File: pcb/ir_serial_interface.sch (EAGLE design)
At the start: 22 parts, among them IC1 PIC18F2550_28W, T1 SFH303

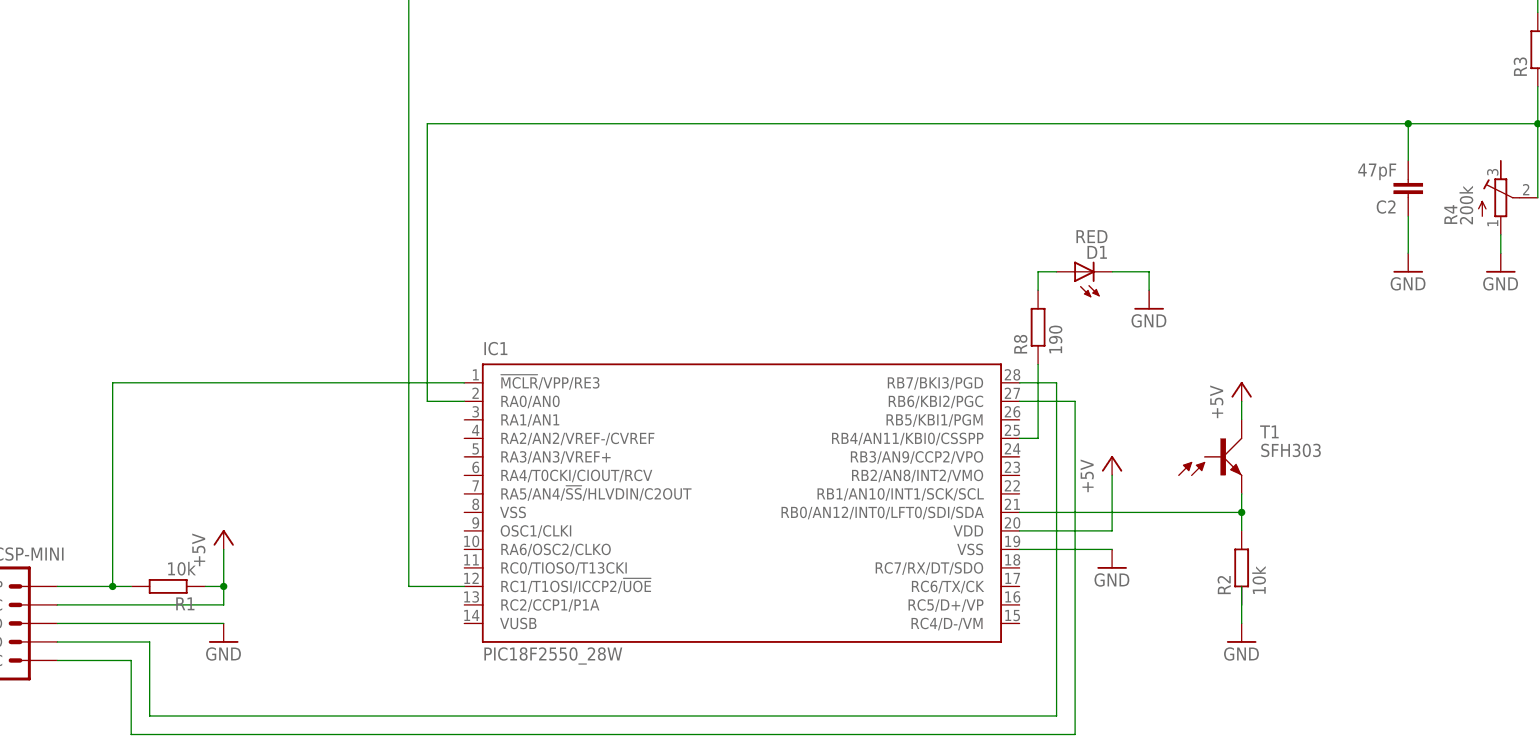
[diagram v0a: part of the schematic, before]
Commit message: RS232_TX working
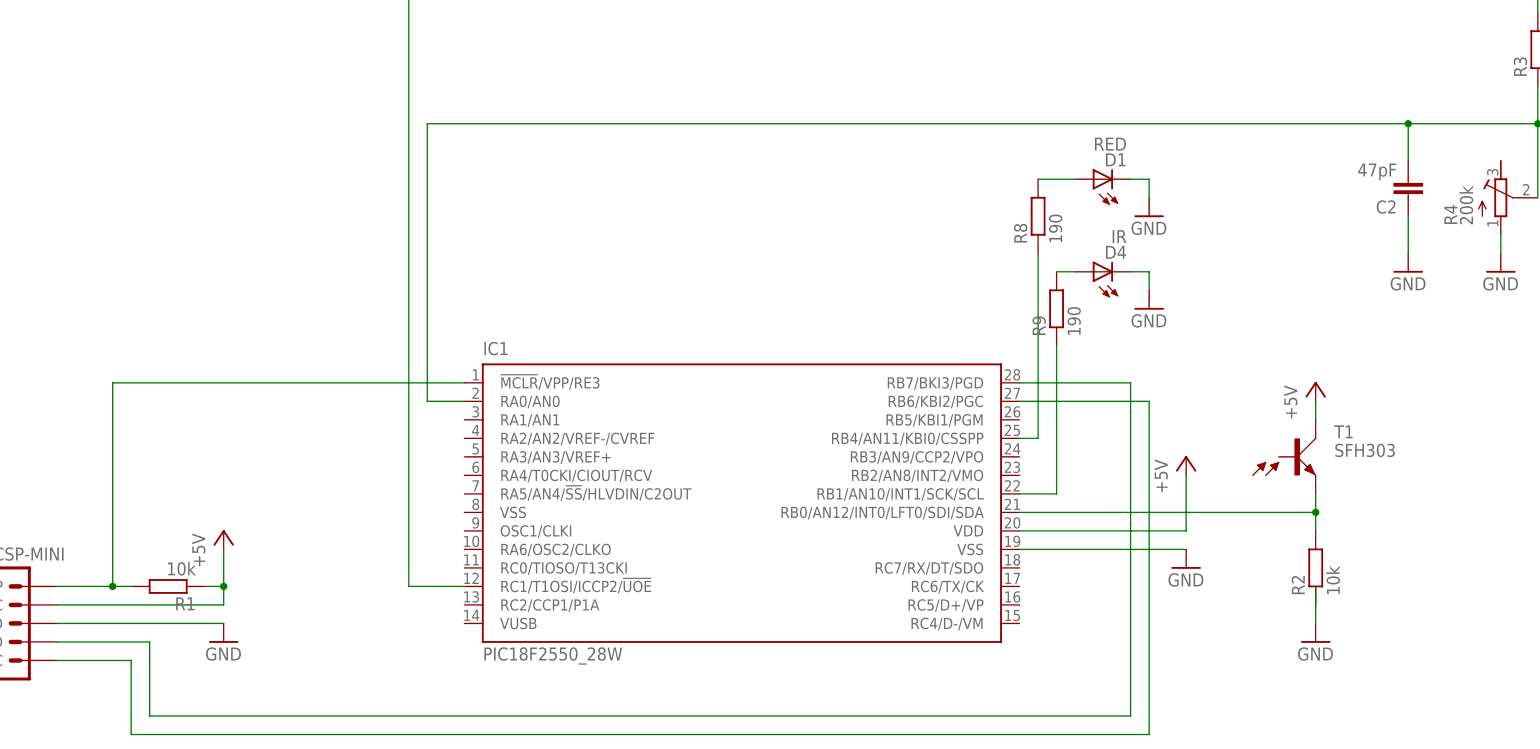
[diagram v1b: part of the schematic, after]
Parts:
- added D4: IR, led:LED3MM
- added R9: 190, resistor:R-EU_M0805
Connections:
- new net N$14: D4.A, R9.2
- new net N$15: IC1.RB1/AN10/INT1/SCK/SCL, R9.1
- net GND: now also D4.C
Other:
- moved on the sheet: D1, R2, R8, T1
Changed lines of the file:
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@@
 <?xml version="1.0" encoding="utf-8"?>
 <!DOCTYPE eagle SYSTEM "eagle.dtd">
-<eagle version="6.5.0">
+<eagle version="6.6.0">
 <drawing>
 <settings>
@@
 <part name="GND10" library="supply1" deviceset="GND" device=""/>
 <part name="R4" library="resistor" deviceset="R-TRIMM" device="3214W" value="200k"/>
+<part name="R9" library="resistor" deviceset="R-EU_" device="M0805" value="190"/>
+<part name="D4" library="led" deviceset="LED" device="3MM" value="IR"/>
+<part name="GND11" library="supply1" deviceset="GND" device=""/>
 </parts>
 <sheets>
@@
 </plain>
 <instances>
-<instance part="T1" gate="G$1" x="160.02" y="27.94"/>
-<instance part="P+1" gate="1" x="144.78" y="27.94"/>
-<instance part="GND1" gate="1" x="144.78" y="12.7"/>
-<instance part="P+2" gate="1" x="162.56" y="38.1"/>
-<instance part="GND2" gate="1" x="162.56" y="2.54"/>
-<instance part="R2" gate="G$1" x="162.56" y="12.7" rot="R90"/>
+<instance part="T1" gate="G$1" x="170.18" y="27.94"/>
+<instance part="P+1" gate="1" x="154.94" y="27.94"/>
+<instance part="GND1" gate="1" x="154.94" y="12.7"/>
+<instance part="P+2" gate="1" x="172.72" y="38.1"/>
+<instance part="GND2" gate="1" x="172.72" y="2.54"/>
+<instance part="R2" gate="G$1" x="172.72" y="12.7" rot="R90"/>
 <instance part="U$1" gate="G$1" x="-7.62" y="5.08" rot="MR0"/>
 <instance part="P+3" gate="1" x="22.86" y="17.78"/>
@@
 <instance part="GND7" gate="1" x="213.36" y="111.76"/>
 <instance part="GND8" gate="1" x="195.58" y="111.76"/>
-<instance part="D1" gate="G$1" x="139.7" y="53.34" rot="R90"/>
-<instance part="GND9" gate="1" x="149.86" y="48.26"/>
-<instance part="R8" gate="G$1" x="134.62" y="45.72" rot="R90"/>
+<instance part="D1" gate="G$1" x="142.24" y="66.04" rot="R90"/>
+<instance part="GND9" gate="1" x="149.86" y="60.96"/>
+<instance part="R8" gate="G$1" x="134.62" y="60.96" rot="R90"/>
 <instance part="BAT1" gate="G$1" x="-2.54" y="114.3"/>
 <instance part="D2" gate="G$1" x="12.7" y="114.3" rot="R180"/>
@@
 <instance part="GND10" gate="1" x="30.48" y="106.68"/>
 <instance part="R4" gate="G$1" x="198.12" y="63.5"/>
+<instance part="R9" gate="G$1" x="137.16" y="48.26" rot="R90"/>
+<instance part="D4" gate="G$1" x="142.24" y="53.34" rot="R90"/>
+<instance part="GND11" gate="1" x="149.86" y="48.26"/>
 </instances>
 <busses>
@@
 <pinref part="P+2" gate="1" pin="+5V"/>
 <pinref part="T1" gate="G$1" pin="C"/>
-<wire x1="162.56" y1="35.56" x2="162.56" y2="33.02" width="0.1524" layer="91"/>
+<wire x1="172.72" y1="35.56" x2="172.72" y2="33.02" width="0.1524" layer="91"/>
 </segment>
 <segment>
@@
 <segment>
 <pinref part="P+1" gate="1" pin="+5V"/>
-<wire x1="144.78" y1="25.4" x2="144.78" y2="17.78" width="0.1524" layer="91"/>
+<wire x1="154.94" y1="25.4" x2="154.94" y2="17.78" width="0.1524" layer="91"/>
 <pinref part="IC1" gate="G$1" pin="VDD"/>
-<wire x1="144.78" y1="17.78" x2="132.08" y2="17.78" width="0.1524" layer="91"/>
+<wire x1="154.94" y1="17.78" x2="132.08" y2="17.78" width="0.1524" layer="91"/>
 </segment>
 <segment>
@@
 <pinref part="GND2" gate="1" pin="GND"/>
 <pinref part="R2" gate="G$1" pin="1"/>
-<wire x1="162.56" y1="5.08" x2="162.56" y2="7.62" width="0.1524" layer="91"/>
-<wire x1="162.56" y1="7.62" x2="162.56" y2="10.16" width="0.1524" layer="91"/>
+<wire x1="172.72" y1="5.08" x2="172.72" y2="7.62" width="0.1524" layer="91"/>
+<wire x1="172.72" y1="7.62" x2="172.72" y2="10.16" width="0.1524" layer="91"/>
 </segment>
 <segment>
@@
 <pinref part="GND1" gate="1" pin="GND"/>
 <pinref part="IC1" gate="G$1" pin="VSS@1"/>
-<wire x1="144.78" y1="15.24" x2="132.08" y2="15.24" width="0.1524" layer="91"/>
+<wire x1="154.94" y1="15.24" x2="132.08" y2="15.24" width="0.1524" layer="91"/>
 </segment>
 <segment>
@@
 <pinref part="D1" gate="G$1" pin="C"/>
 <pinref part="GND9" gate="1" pin="GND"/>
-<wire x1="144.78" y1="53.34" x2="149.86" y2="53.34" width="0.1524" layer="91"/>
-<wire x1="149.86" y1="53.34" x2="149.86" y2="50.8" width="0.1524" layer="91"/>
+<wire x1="147.32" y1="66.04" x2="149.86" y2="66.04" width="0.1524" layer="91"/>
+<wire x1="149.86" y1="66.04" x2="149.86" y2="63.5" width="0.1524" layer="91"/>
 </segment>
 <segment>
@@
 <wire x1="198.12" y1="58.42" x2="198.12" y2="55.88" width="0.1524" layer="91"/>
 </segment>
+<segment>
+<pinref part="D4" gate="G$1" pin="C"/>
+<pinref part="GND11" gate="1" pin="GND"/>
+<wire x1="147.32" y1="53.34" x2="149.86" y2="53.34" width="0.1524" layer="91"/>
+<wire x1="149.86" y1="53.34" x2="149.86" y2="50.8" width="0.1524" layer="91"/>
+</segment>
 </net>
 <net name="N$1" class="0">
@@
 <pinref part="R2" gate="G$1" pin="2"/>
 <pinref part="T1" gate="G$1" pin="E"/>
-<wire x1="162.56" y1="17.78" x2="162.56" y2="20.32" width="0.1524" layer="91"/>
+<wire x1="172.72" y1="17.78" x2="172.72" y2="20.32" width="0.1524" layer="91"/>
 <pinref part="IC1" gate="G$1" pin="RB0/AN12/INT0/LFT0/SDI/SDA"/>
-<wire x1="162.56" y1="20.32" x2="162.56" y2="22.86" width="0.1524" layer="91"/>
-<wire x1="132.08" y1="20.32" x2="162.56" y2="20.32" width="0.1524" layer="91"/>
-<junction x="162.56" y="20.32"/>
+<wire x1="172.72" y1="20.32" x2="172.72" y2="22.86" width="0.1524" layer="91"/>
+<wire x1="132.08" y1="20.32" x2="172.72" y2="20.32" width="0.1524" layer="91"/>
+<junction x="172.72" y="20.32"/>
 </segment>
 </net>
@@
 <wire x1="0" y1="2.54" x2="12.7" y2="2.54" width="0.1524" layer="91"/>
 <wire x1="12.7" y1="2.54" x2="12.7" y2="-7.62" width="0.1524" layer="91"/>
-<wire x1="12.7" y1="-7.62" x2="137.16" y2="-7.62" width="0.1524" layer="91"/>
-<wire x1="137.16" y1="-7.62" x2="137.16" y2="38.1" width="0.1524" layer="91"/>
+<wire x1="12.7" y1="-7.62" x2="147.32" y2="-7.62" width="0.1524" layer="91"/>
+<wire x1="147.32" y1="-7.62" x2="147.32" y2="38.1" width="0.1524" layer="91"/>
 <pinref part="IC1" gate="G$1" pin="RB7/BKI3/PGD"/>
-<wire x1="137.16" y1="38.1" x2="132.08" y2="38.1" width="0.1524" layer="91"/>
+<wire x1="147.32" y1="38.1" x2="132.08" y2="38.1" width="0.1524" layer="91"/>
 </segment>
 </net>
@@
 <pinref part="U$1" gate="G$1" pin="PGC"/>
 <wire x1="10.16" y1="0" x2="0" y2="0" width="0.1524" layer="91"/>
-<wire x1="10.16" y1="-10.16" x2="139.7" y2="-10.16" width="0.1524" layer="91"/>
-<wire x1="139.7" y1="-10.16" x2="139.7" y2="35.56" width="0.1524" layer="91"/>
+<wire x1="10.16" y1="-10.16" x2="149.86" y2="-10.16" width="0.1524" layer="91"/>
+<wire x1="149.86" y1="-10.16" x2="149.86" y2="35.56" width="0.1524" layer="91"/>
 <pinref part="IC1" gate="G$1" pin="RB6/KBI2/PGC"/>
-<wire x1="139.7" y1="35.56" x2="132.08" y2="35.56" width="0.1524" layer="91"/>
+<wire x1="149.86" y1="35.56" x2="132.08" y2="35.56" width="0.1524" layer="91"/>
 </segment>
 </net>
@@
 <segment>
 <pinref part="D1" gate="G$1" pin="A"/>
-<wire x1="134.62" y1="53.34" x2="137.16" y2="53.34" width="0.1524" layer="91"/>
 <pinref part="R8" gate="G$1" pin="2"/>
-<wire x1="134.62" y1="53.34" x2="134.62" y2="50.8" width="0.1524" layer="91"/>
+<wire x1="139.7" y1="66.04" x2="134.62" y2="66.04" width="0.1524" layer="91"/>
 </segment>
 </net>
@@
 <wire x1="132.08" y1="30.48" x2="134.62" y2="30.48" width="0.1524" layer="91"/>
 <pinref part="R8" gate="G$1" pin="1"/>
-<wire x1="134.62" y1="40.64" x2="134.62" y2="30.48" width="0.1524" layer="91"/>
+<wire x1="134.62" y1="55.88" x2="134.62" y2="30.48" width="0.1524" layer="91"/>
 </segment>
 </net>
@@
 </segment>
 </net>
+<net name="N$14" class="0">
+<segment>
+<pinref part="D4" gate="G$1" pin="A"/>
+<pinref part="R9" gate="G$1" pin="2"/>
+<wire x1="139.7" y1="53.34" x2="137.16" y2="53.34" width="0.1524" layer="91"/>
+</segment>
+</net>
+<net name="N$15" class="0">
+<segment>
+<pinref part="R9" gate="G$1" pin="1"/>
+<wire x1="137.16" y1="43.18" x2="137.16" y2="22.86" width="0.1524" layer="91"/>
+<pinref part="IC1" gate="G$1" pin="RB1/AN10/INT1/SCK/SCL"/>
+<wire x1="137.16" y1="22.86" x2="132.08" y2="22.86" width="0.1524" layer="91"/>
+</segment>
+</net>

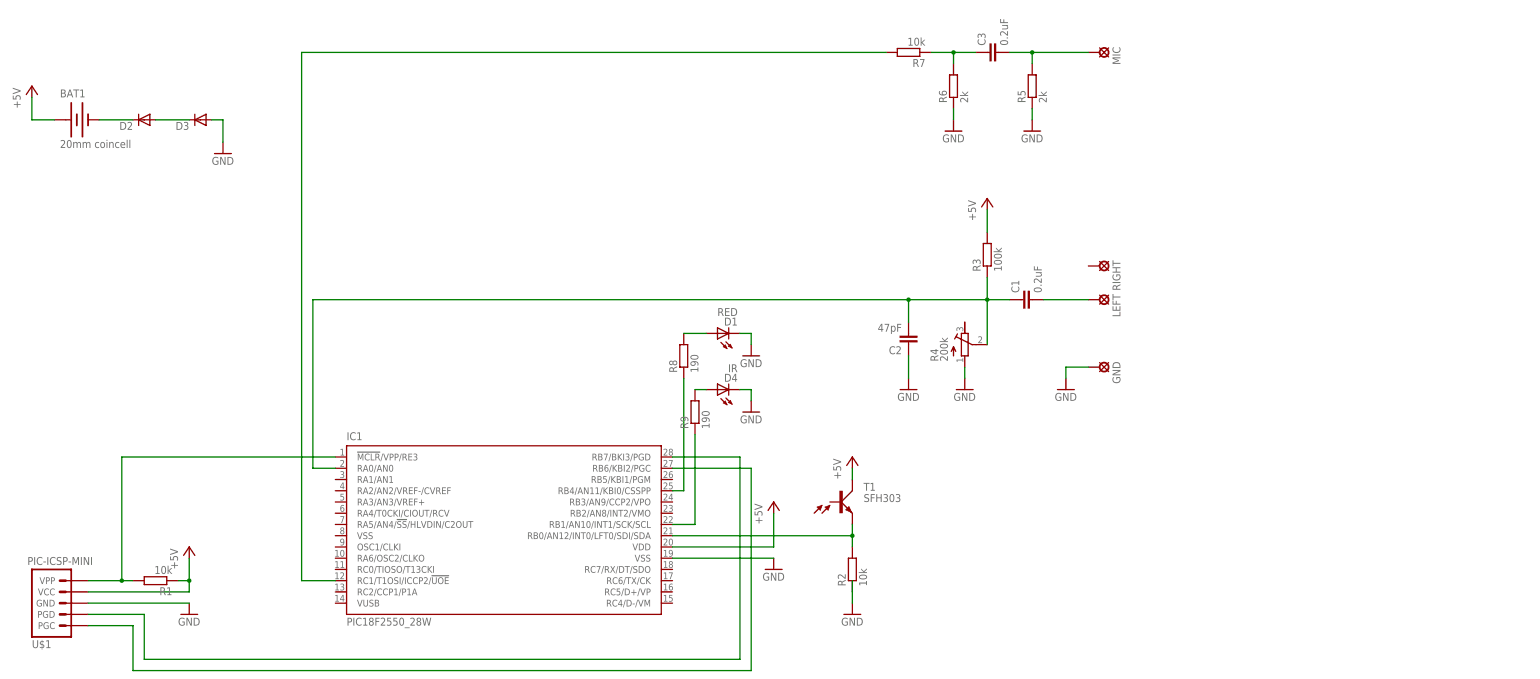
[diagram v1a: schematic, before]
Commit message: PCB: R channel enables MeterLogger
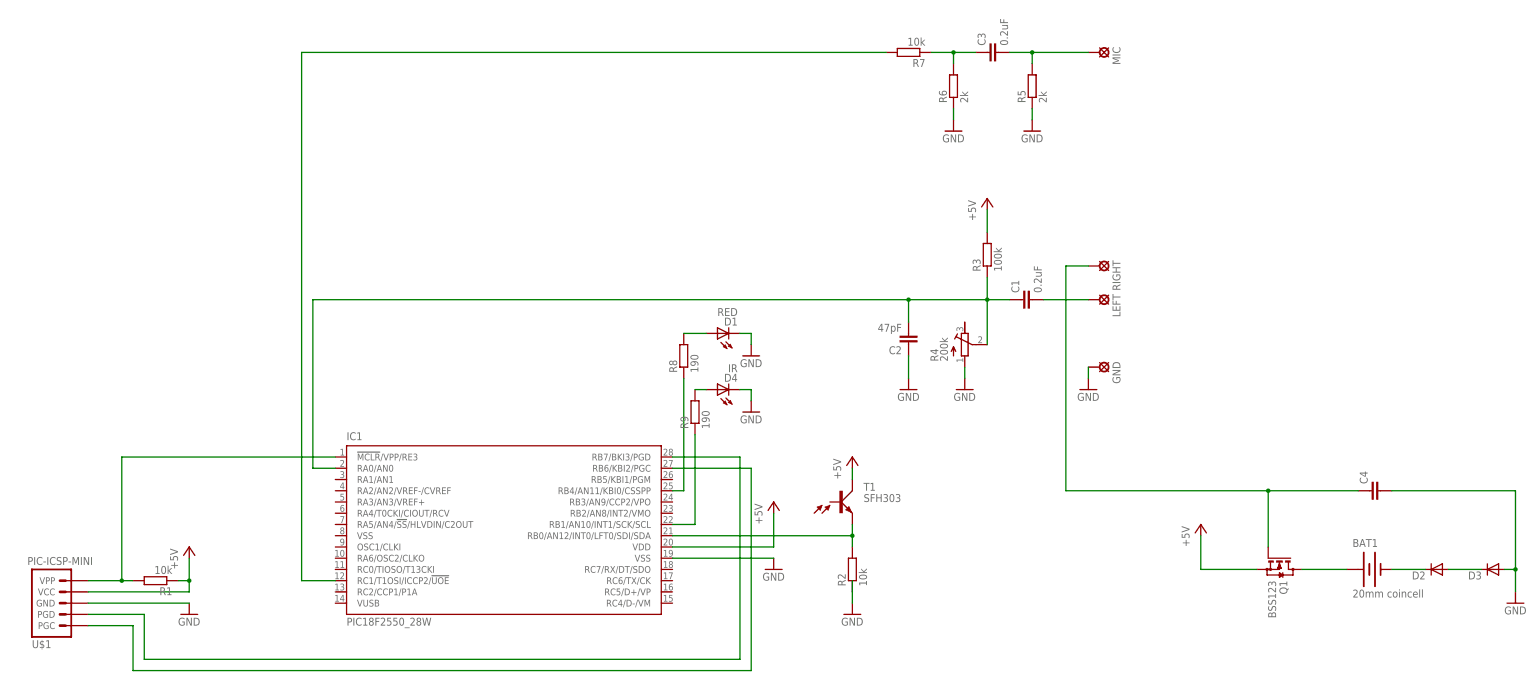
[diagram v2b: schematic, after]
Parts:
- added C4: (no value), rcl:C-EUC0805
- added Q1: BSS123, transistor-small-signal:BSS123
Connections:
- new net N$16: BAT1.+, Q1.D
- new net N$17: C4.1, Q1.G, RIGHT.MP
- net +5V: now also Q1.S; no longer BAT1.+
- net GND: now also C4.2
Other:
- moved on the sheet: BAT1, D2, D3
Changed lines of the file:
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@@
 <part name="D4" library="led" deviceset="LED" device="3MM" value="IR"/>
 <part name="GND11" library="supply1" deviceset="GND" device=""/>
+<part name="Q1" library="transistor-small-signal" deviceset="BSS123" device=""/>
+<part name="C4" library="rcl" deviceset="C-EU" device="C0805"/>
 </parts>
 <sheets>
@@
 <instance part="C2" gate="G$1" x="185.42" y="66.04" rot="R180"/>
 <instance part="P+4" gate="1" x="203.2" y="96.52"/>
-<instance part="GND4" gate="1" x="220.98" y="53.34"/>
+<instance part="GND4" gate="1" x="226.06" y="53.34"/>
 <instance part="GND5" gate="1" x="198.12" y="53.34"/>
 <instance part="GND6" gate="1" x="185.42" y="53.34"/>
@@
 <instance part="GND9" gate="1" x="149.86" y="60.96"/>
 <instance part="R8" gate="G$1" x="134.62" y="60.96" rot="R90"/>
-<instance part="BAT1" gate="G$1" x="-2.54" y="114.3"/>
-<instance part="D2" gate="G$1" x="12.7" y="114.3" rot="R180"/>
-<instance part="D3" gate="G$1" x="25.4" y="114.3" rot="R180"/>
-<instance part="P+5" gate="1" x="-12.7" y="121.92"/>
-<instance part="GND10" gate="1" x="30.48" y="106.68"/>
+<instance part="BAT1" gate="G$1" x="289.56" y="12.7"/>
+<instance part="D2" gate="G$1" x="304.8" y="12.7" rot="R180"/>
+<instance part="D3" gate="G$1" x="317.5" y="12.7" rot="R180"/>
+<instance part="P+5" gate="1" x="251.46" y="22.86"/>
+<instance part="GND10" gate="1" x="322.58" y="5.08"/>
 <instance part="R4" gate="G$1" x="198.12" y="63.5"/>
 <instance part="R9" gate="G$1" x="137.16" y="48.26" rot="R90"/>
 <instance part="D4" gate="G$1" x="142.24" y="53.34" rot="R90"/>
 <instance part="GND11" gate="1" x="149.86" y="48.26"/>
+<instance part="Q1" gate="G$1" x="269.24" y="12.7" rot="R270"/>
+<instance part="C4" gate="G$1" x="289.56" y="30.48" rot="R90"/>
 </instances>
 <busses>
@@
 <segment>
 <pinref part="P+5" gate="1" pin="+5V"/>
-<wire x1="-12.7" y1="119.38" x2="-12.7" y2="114.3" width="0.1524" layer="91"/>
-<pinref part="BAT1" gate="G$1" pin="+"/>
-<wire x1="-12.7" y1="114.3" x2="-7.62" y2="114.3" width="0.1524" layer="91"/>
+<wire x1="251.46" y1="20.32" x2="251.46" y2="12.7" width="0.1524" layer="91"/>
+<pinref part="Q1" gate="G$1" pin="S"/>
+<wire x1="251.46" y1="12.7" x2="264.16" y2="12.7" width="0.1524" layer="91"/>
 </segment>
 </net>
@@
 <pinref part="GND" gate="1" pin="MP"/>
 <pinref part="GND4" gate="1" pin="GND"/>
-<wire x1="226.06" y1="58.42" x2="220.98" y2="58.42" width="0.1524" layer="91"/>
-<wire x1="220.98" y1="58.42" x2="220.98" y2="55.88" width="0.1524" layer="91"/>
+<wire x1="226.06" y1="58.42" x2="226.06" y2="55.88" width="0.1524" layer="91"/>
 </segment>
 <segment>
@@
 <pinref part="D3" gate="G$1" pin="A"/>
 <pinref part="GND10" gate="1" pin="GND"/>
-<wire x1="27.94" y1="114.3" x2="30.48" y2="114.3" width="0.1524" layer="91"/>
-<wire x1="30.48" y1="114.3" x2="30.48" y2="109.22" width="0.1524" layer="91"/>
+<wire x1="320.04" y1="12.7" x2="322.58" y2="12.7" width="0.1524" layer="91"/>
+<wire x1="322.58" y1="12.7" x2="322.58" y2="7.62" width="0.1524" layer="91"/>
+<pinref part="C4" gate="G$1" pin="2"/>
+<wire x1="294.64" y1="30.48" x2="322.58" y2="30.48" width="0.1524" layer="91"/>
+<wire x1="322.58" y1="30.48" x2="322.58" y2="12.7" width="0.1524" layer="91"/>
+<junction x="322.58" y="12.7"/>
 </segment>
 <segment>
@@
 <pinref part="BAT1" gate="G$1" pin="-"/>
 <pinref part="D2" gate="G$1" pin="C"/>
-<wire x1="2.54" y1="114.3" x2="10.16" y2="114.3" width="0.1524" layer="91"/>
+<wire x1="294.64" y1="12.7" x2="302.26" y2="12.7" width="0.1524" layer="91"/>
 </segment>
 </net>
@@
 <pinref part="D2" gate="G$1" pin="A"/>
 <pinref part="D3" gate="G$1" pin="C"/>
-<wire x1="15.24" y1="114.3" x2="22.86" y2="114.3" width="0.1524" layer="91"/>
+<wire x1="307.34" y1="12.7" x2="314.96" y2="12.7" width="0.1524" layer="91"/>
 </segment>
 </net>
@@
 </segment>
 </net>
+<net name="N$16" class="0">
+<segment>
+<pinref part="Q1" gate="G$1" pin="D"/>
+<pinref part="BAT1" gate="G$1" pin="+"/>
+<wire x1="274.32" y1="12.7" x2="284.48" y2="12.7" width="0.1524" layer="91"/>
+</segment>
+</net>
+<net name="N$17" class="0">
+<segment>
+<pinref part="RIGHT" gate="1" pin="MP"/>
+<wire x1="226.06" y1="81.28" x2="220.98" y2="81.28" width="0.1524" layer="91"/>
+<wire x1="220.98" y1="81.28" x2="220.98" y2="30.48" width="0.1524" layer="91"/>
+<pinref part="Q1" gate="G$1" pin="G"/>
+<wire x1="220.98" y1="30.48" x2="266.7" y2="30.48" width="0.1524" layer="91"/>
+<wire x1="266.7" y1="30.48" x2="266.7" y2="17.78" width="0.1524" layer="91"/>
+<pinref part="C4" gate="G$1" pin="1"/>
+<wire x1="266.7" y1="30.48" x2="287.02" y2="30.48" width="0.1524" layer="91"/>
+<junction x="266.7" y="30.48"/>
+</segment>
+</net>
